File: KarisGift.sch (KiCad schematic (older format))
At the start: 35 parts

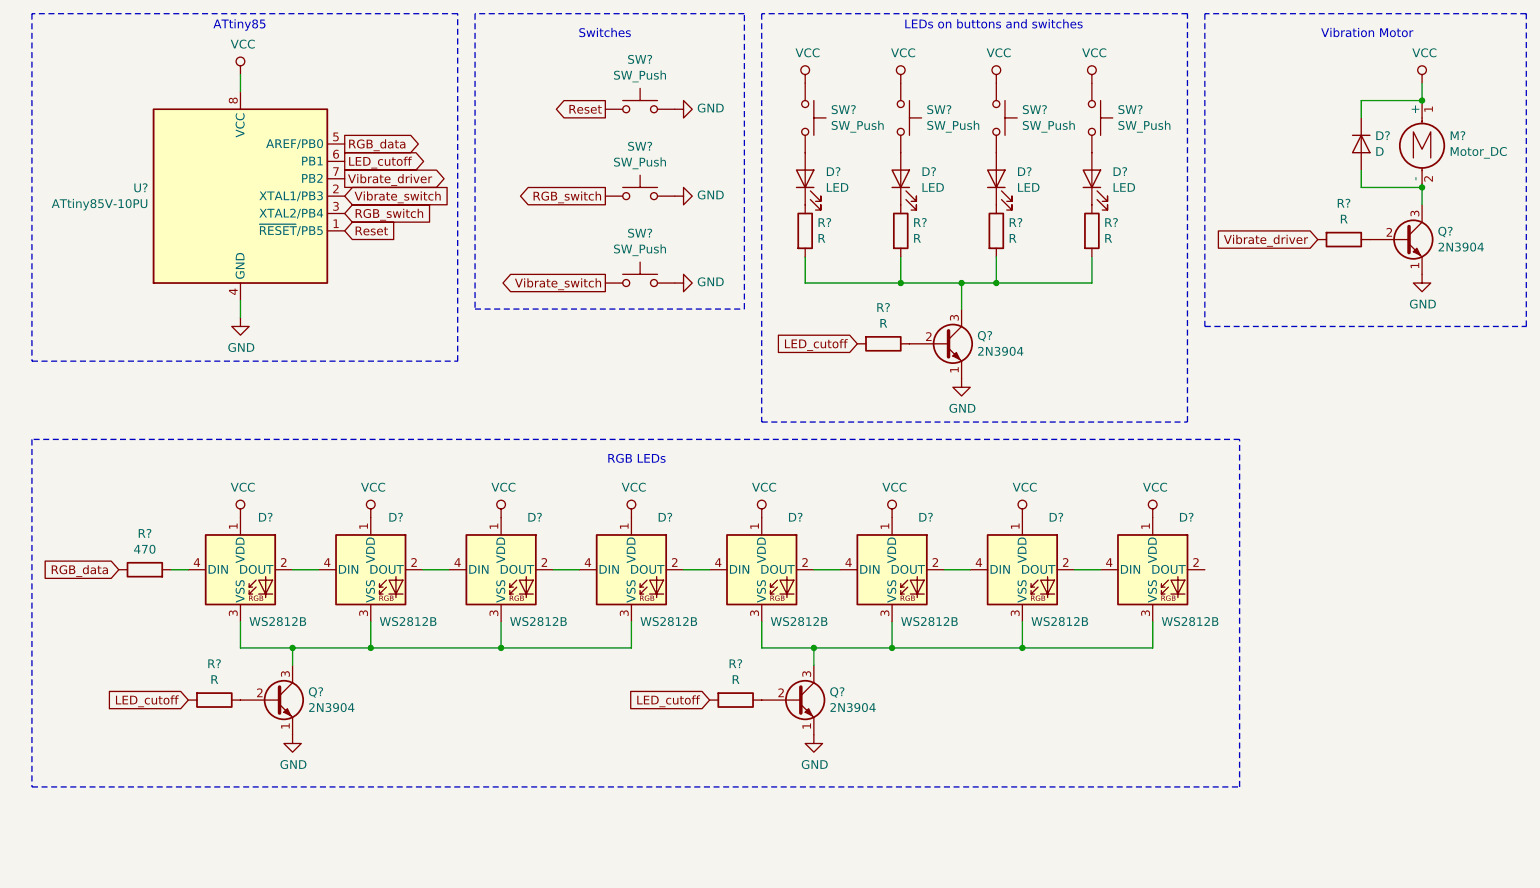
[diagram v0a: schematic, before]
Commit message: Updated RGB LEDs block to not move ground reference on data signal.
Added pull up/down resisters for transistors.
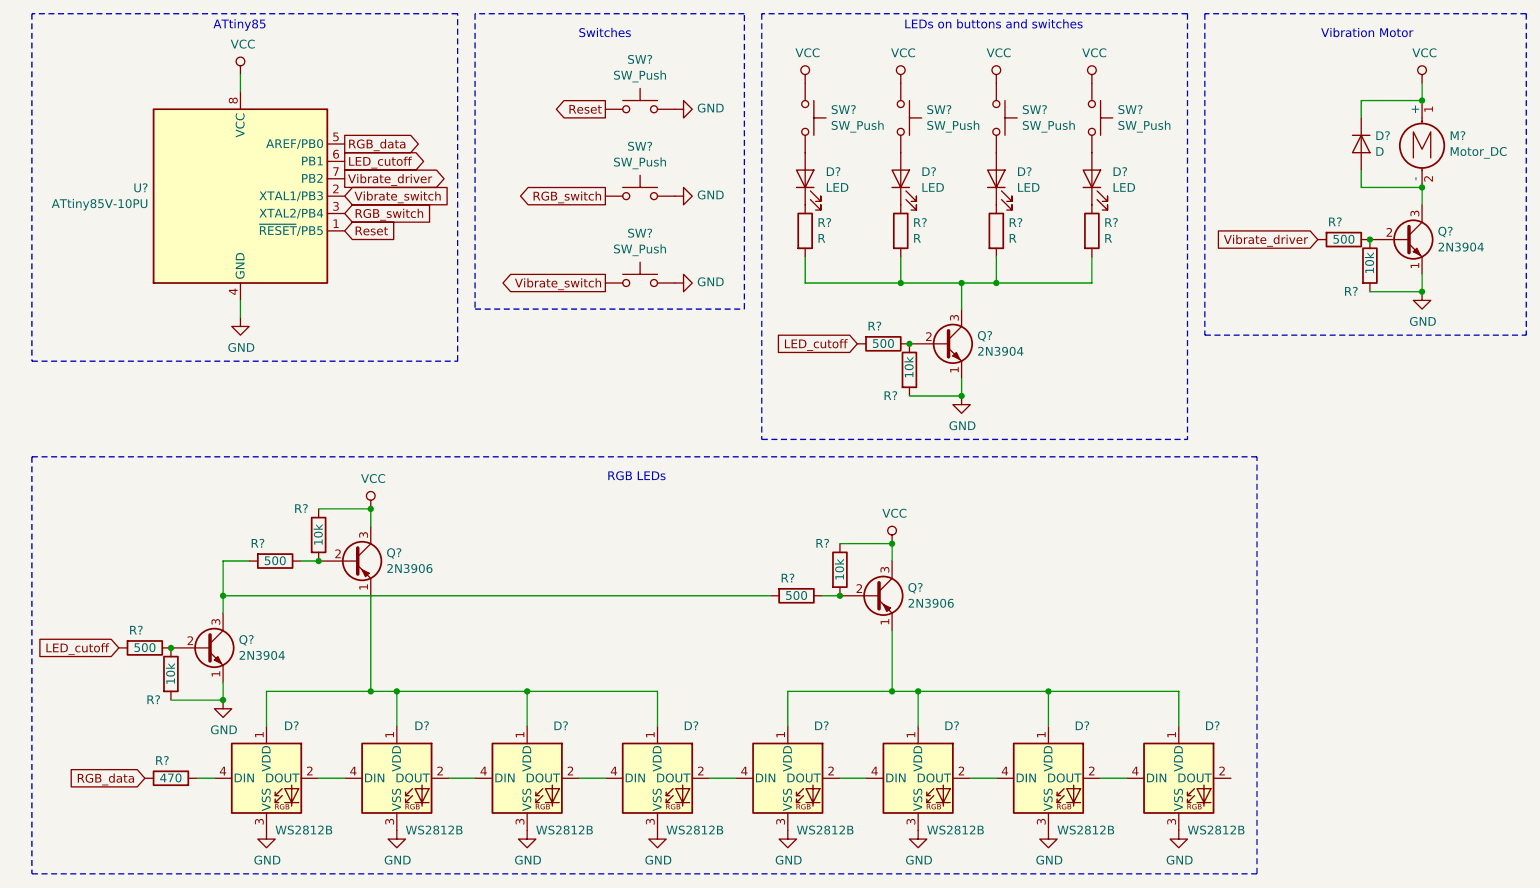
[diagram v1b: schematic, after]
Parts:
- removed Q?: 2N3904, Package_TO_SOT_THT:TO-92_Inline, symbol Transistor_BJT:2N3904
- removed R?: R, symbol Device:R
- added Q? (x2): 2N3906, Package_TO_SOT_THT:TO-92_Inline, symbol Transistor_BJT:2N3906
- added R? (x5): 10k, symbol Device:R
- added R? (x2): 500, symbol Device:R
- R? (x3): value R -> 500
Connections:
- net GND: now also D?.3 (VSS), D?.3 (VSS), D?.3 (VSS), D?.3 (VSS), D?.3 (VSS), D?.3 (VSS), D?.3 (VSS), D?.3 (VSS), R?.2, R?.2, R?.2
- net VCC: now also Q?.3 (C), Q?.3 (C), R?.1, R?.1; no longer D?.1 (VDD), D?.1 (VDD), D?.1 (VDD), D?.1 (VDD), D?.1 (VDD), D?.1 (VDD), D?.1 (VDD), D?.1 (VDD)
- net at Q?.2 (B), R?.1: now also R?.1 (x3)
- new net: D?.1 (VDD), D?.1 (VDD), D?.1 (VDD), D?.1 (VDD), Q?.1 (E) (x2)
- new net: Q?.3 (C), R?.2, R?.2
- new net: Q?.2 (B), R?.1, R?.2 (x2)
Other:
- moved on the sheet: D?, Q?, R?

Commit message: I can't believe it works! The code works!
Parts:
- U?: symbol MCU_Microchip_ATtiny:ATtiny85V-10PU -> KarisGift-rescue:ATtiny85V-10PU-MCU_Microchip_ATtiny
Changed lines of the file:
@@
 EESchema Schematic File Version 4
+LIBS:KarisGift-cache
 EELAYER 30 0
 EELAYER END
@@
 $EndDescr
 $Comp
-L MCU_Microchip_ATtiny:ATtiny85V-10PU U?
+L KarisGift-rescue:ATtiny85V-10PU-MCU_Microchip_ATtiny U?
 U 1 1 5FDE0C7F
 P 1900 1700

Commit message: Updated schematic to use just one PNP transistor for RGB LEDs.
Started the long process of cleaning up the code.
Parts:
- removed Q?: 2N3906, Package_TO_SOT_THT:TO-92_Inline, symbol Transistor_BJT:2N3906
- removed R?: 10k, symbol Device:R
- removed R?: 500, symbol Device:R
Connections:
- net at D?.1 (VDD), D?.1 (VDD), D?.1 (VDD)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: now also D?.1 (VDD), D?.1 (VDD), D?.1 (VDD), D?.1 (VDD)
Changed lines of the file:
@@
 Connection ~ 3550 4550
-$Comp
-L power:VCC #PWR?
-U 1 1 5FFC19B6
-P 5650 3700
-F 0 "#PWR?" H 5650 3550 50  0001 C CNN
-F 1 "VCC" H 5665 3873 50  0000 C CNN
-F 2 "" H 5650 3700 50  0001 C CNN
-F 3 "" H 5650 3700 50  0001 C CNN
-	1    5650 3700
-	1    0    0    -1
-$EndComp
-$Comp
-L Transistor_BJT:2N3906 Q?
-U 1 1 5FFC19BC
-P 5550 4000
-F 0 "Q?" H 5740 4046 50  0000 L CNN
-F 1 "2N3906" H 5740 3955 50  0000 L CNN
-F 2 "Package_TO_SOT_THT:TO-92_Inline" H 5750 3925 50  0001 L CIN
-F 3 "https://www.fairchildsemi.com/datasheets/2N/2N3906.pdf" H 5550 4000 50  0001 L CNN
-	1    5550 4000
-	1    0    0    -1
-$EndComp
-$Comp
-L Device:R R?
-U 1 1 5FFC19C2
-P 5350 3850
-F 0 "R?" H 5250 4000 50  0000 C CNN
-F 1 "10k" V 5350 3850 50  0000 C CNN
-F 2 "" V 5280 3850 50  0001 C CNN
-F 3 "~" H 5350 3850 50  0001 C CNN
-	1    5350 3850
-	1    0    0    -1
-$EndComp
-Wire Wire Line
-	5350 3700 5650 3700
-Wire Wire Line
-	5650 3700 5650 3800
-Connection ~ 5650 3700
-$Comp
-L Device:R R?
-U 1 1 5FFC19CB
-P 5100 4000
-F 0 "R?" V 5000 3950 50  0000 C CNN
-F 1 "500" V 5100 4000 50  0000 C CNN
-F 2 "" V 5030 4000 50  0001 C CNN
-F 3 "~" H 5100 4000 50  0001 C CNN
-	1    5100 4000
-	0    1    1    0
-$EndComp
-Wire Wire Line
-	5350 4000 5250 4000
-Connection ~ 5350 4000
 $Comp
 L power:GND #PWR?
@@
 	7300 4550 7300 4750
 Connection ~ 6550 4550
-Wire Wire Line
-	5050 4550 5650 4550
-Wire Wire Line
-	1800 3800 1800 4000
-Connection ~ 1800 4000
-Wire Wire Line
-	1800 4000 1800 4100
-Wire Wire Line
-	5650 4200 5650 4550
-Connection ~ 5650 4550
-Wire Wire Line
-	5650 4550 5800 4550
 $Comp
 L Device:R R?
@@
 	4900 650  4900 3100
 Wire Wire Line
-	1800 4000 4950 4000
+	5050 4550 5800 4550
+Wire Wire Line
+	1800 3800 1800 4100
+Wire Wire Line
+	5050 4550 4300 4550
+Connection ~ 5050 4550
+Connection ~ 4300 4550
 $EndSCHEMATC

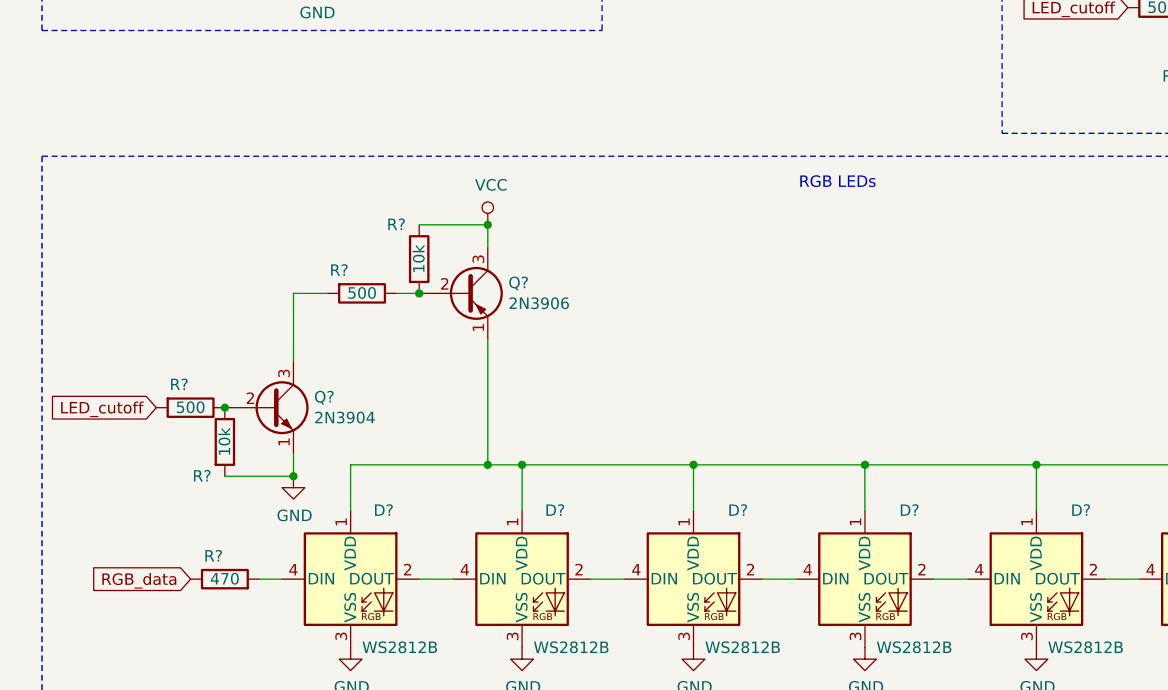
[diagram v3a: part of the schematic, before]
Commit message: Fixed backwards PNP transistor running the RGB LEDs (Thanks Ron!)
Some more code cleanup.
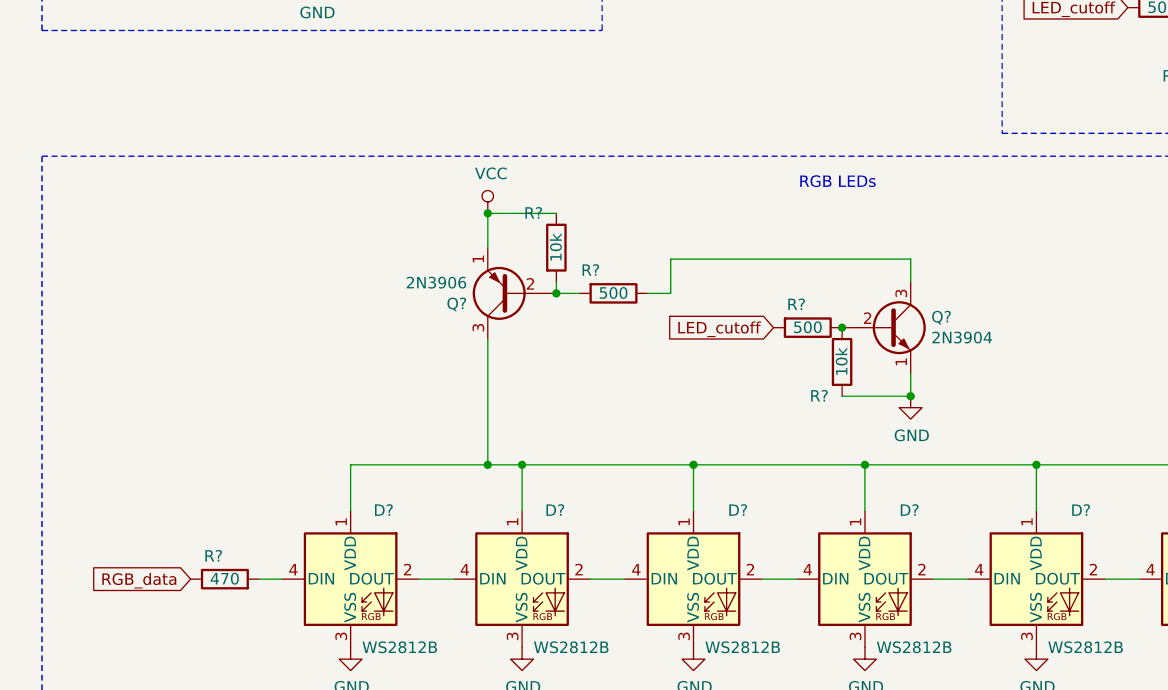
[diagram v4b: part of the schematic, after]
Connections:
- net VCC: now also Q?.1 (E); no longer Q?.3 (C)
- net at D?.1 (VDD), D?.1 (VDD), D?.1 (VDD)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: now also Q?.3 (C); no longer Q?.1 (E)
- net at Q?.3 (C): now also R?.1; no longer R?.2
- net at Q?.2 (B), R?.2: now also R?.2; no longer R?.1
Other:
- moved on the sheet: Q?, R?
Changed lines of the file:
@@
 L power:VCC #PWR?
 U 1 1 5FE03943
-P 2650 3500
-F 0 "#PWR?" H 2650 3350 50  0001 C CNN
-F 1 "VCC" H 2665 3673 50  0000 C CNN
-F 2 "" H 2650 3500 50  0001 C CNN
-F 3 "" H 2650 3500 50  0001 C CNN
-	1    2650 3500
+P 2650 3450
+F 0 "#PWR?" H 2650 3300 50  0001 C CNN
+F 1 "VCC" H 2665 3623 50  0000 C CNN
+F 2 "" H 2650 3450 50  0001 C CNN
+F 3 "" H 2650 3450 50  0001 C CNN
+	1    2650 3450
 	1    0    0    -1
 $EndComp
@@
 L Device:R R?
 U 1 1 5FE0932F
-P 1350 4300
-F 0 "R?" V 1250 4250 50  0000 C CNN
-F 1 "500" V 1350 4300 50  0000 C CNN
-F 2 "" V 1280 4300 50  0001 C CNN
-F 3 "~" H 1350 4300 50  0001 C CNN
-	1    1350 4300
+P 4050 3950
+F 0 "R?" V 3950 3900 50  0000 C CNN
+F 1 "500" V 4050 3950 50  0000 C CNN
+F 2 "" V 3980 3950 50  0001 C CNN
+F 3 "~" H 4050 3950 50  0001 C CNN
+	1    4050 3950
 	0    1    1    0
 $EndComp
@@
 L power:GND #PWR?
 U 1 1 5FE09335
-P 1800 4600
-F 0 "#PWR?" H 1800 4350 50  0001 C CNN
-F 1 "GND" H 1805 4427 50  0000 C CNN
-F 2 "" H 1800 4600 50  0001 C CNN
-F 3 "" H 1800 4600 50  0001 C CNN
-	1    1800 4600
+P 4500 4250
+F 0 "#PWR?" H 4500 4000 50  0001 C CNN
+F 1 "GND" H 4505 4077 50  0000 C CNN
+F 2 "" H 4500 4250 50  0001 C CNN
+F 3 "" H 4500 4250 50  0001 C CNN
+	1    4500 4250
 	1    0    0    -1
 $EndComp
@@
 Wire Wire Line
 	1650 5050 1750 5050
-Text GLabel 1200 4300 0    50   Input ~ 0
+Text GLabel 3900 3950 0    50   Input ~ 0
 LED_cutoff
 Text Notes 4350 3350 2    50   ~ 0
@@
 L Transistor_BJT:2N3904 Q?
 U 1 1 5FE09329
-P 1700 4300
-F 0 "Q?" H 1890 4346 50  0000 L CNN
-F 1 "2N3904" H 1890 4255 50  0000 L CNN
-F 2 "Package_TO_SOT_THT:TO-92_Inline" H 1900 4225 50  0001 L CIN
-F 3 "https://www.fairchildsemi.com/datasheets/2N/2N3904.pdf" H 1700 4300 50  0001 L CNN
-	1    1700 4300
+P 4400 3950
+F 0 "Q?" H 4590 3996 50  0000 L CNN
+F 1 "2N3904" H 4590 3905 50  0000 L CNN
+F 2 "Package_TO_SOT_THT:TO-92_Inline" H 4600 3875 50  0001 L CIN
+F 3 "https://www.fairchildsemi.com/datasheets/2N/2N3904.pdf" H 4400 3950 50  0001 L CNN
+	1    4400 3950
 	1    0    0    -1
 $EndComp
@@
 L Transistor_BJT:2N3906 Q?
 U 1 1 5FFA5010
-P 2550 3800
-F 0 "Q?" H 2740 3846 50  0000 L CNN
-F 1 "2N3906" H 2740 3755 50  0000 L CNN
-F 2 "Package_TO_SOT_THT:TO-92_Inline" H 2750 3725 50  0001 L CIN
-F 3 "https://www.fairchildsemi.com/datasheets/2N/2N3906.pdf" H 2550 3800 50  0001 L CNN
-	1    2550 3800
-	1    0    0    -1
+P 2750 3800
+F 0 "Q?" H 2940 3846 50  0000 L CNN
+F 1 "2N3906" H 2940 3755 50  0000 L CNN
+F 2 "Package_TO_SOT_THT:TO-92_Inline" H 2950 3725 50  0001 L CIN
+F 3 "https://www.fairchildsemi.com/datasheets/2N/2N3906.pdf" H 2750 3800 50  0001 L CNN
+	1    2750 3800
+	-1   0    0    1
 $EndComp
 $Comp
 L Device:R R?
 U 1 1 5FFA603B
-P 2350 3650
-F 0 "R?" H 2250 3800 50  0000 C CNN
-F 1 "10k" V 2350 3650 50  0000 C CNN
-F 2 "" V 2280 3650 50  0001 C CNN
-F 3 "~" H 2350 3650 50  0001 C CNN
-	1    2350 3650
-	1    0    0    -1
-$EndComp
-Wire Wire Line
-	2350 3500 2650 3500
-Wire Wire Line
-	2650 3500 2650 3600
-Connection ~ 2650 3500
+P 2950 3600
+F 0 "R?" H 2850 3750 50  0000 C CNN
+F 1 "10k" V 2950 3600 50  0000 C CNN
+F 2 "" V 2880 3600 50  0001 C CNN
+F 3 "~" H 2950 3600 50  0001 C CNN
+	1    2950 3600
+	1    0    0    -1
+$EndComp
 $Comp
 L Device:R R?
 U 1 1 5FFAFFBD
-P 2100 3800
-F 0 "R?" V 2000 3700 50  0000 C CNN
-F 1 "500" V 2100 3800 50  0000 C CNN
-F 2 "" V 2030 3800 50  0001 C CNN
-F 3 "~" H 2100 3800 50  0001 C CNN
-	1    2100 3800
+P 3200 3800
+F 0 "R?" V 3100 3700 50  0000 C CNN
+F 1 "500" V 3200 3800 50  0000 C CNN
+F 2 "" V 3130 3800 50  0001 C CNN
+F 3 "~" H 3200 3800 50  0001 C CNN
+	1    3200 3800
 	0    1    1    0
 $EndComp
-Wire Wire Line
-	2350 3800 2250 3800
-Connection ~ 2350 3800
-Wire Wire Line
-	1950 3800 1800 3800
 $Comp
 L power:GND #PWR?
@@
 L Device:R R?
 U 1 1 5FFDCB12
-P 1500 4450
-F 0 "R?" H 1400 4300 50  0000 C CNN
-F 1 "10k" V 1500 4450 50  0000 C CNN
-F 2 "" V 1430 4450 50  0001 C CNN
-F 3 "~" H 1500 4450 50  0001 C CNN
-	1    1500 4450
-	1    0    0    -1
-$EndComp
-Connection ~ 1500 4300
-Wire Wire Line
-	1500 4600 1800 4600
-Wire Wire Line
-	1800 4500 1800 4600
-Connection ~ 1800 4600
+P 4200 4100
+F 0 "R?" H 4100 3950 50  0000 C CNN
+F 1 "10k" V 4200 4100 50  0000 C CNN
+F 2 "" V 4130 4100 50  0001 C CNN
+F 3 "~" H 4200 4100 50  0001 C CNN
+	1    4200 4100
+	1    0    0    -1
+$EndComp
+Connection ~ 4200 3950
+Wire Wire Line
+	4200 4250 4500 4250
+Wire Wire Line
+	4500 4150 4500 4250
+Connection ~ 4500 4250
 Wire Notes Line
 	700  5600 7750 5600
@@
 	5050 4550 5800 4550
 Wire Wire Line
-	1800 3800 1800 4100
-Wire Wire Line
 	5050 4550 4300 4550
 Connection ~ 5050 4550
 Connection ~ 4300 4550
+Wire Wire Line
+	2950 3450 2650 3450
+Connection ~ 2650 3450
+Wire Wire Line
+	2650 3450 2650 3600
+Wire Wire Line
+	2950 3750 2950 3800
+Wire Wire Line
+	2950 3800 3050 3800
+Connection ~ 2950 3800
+Wire Wire Line
+	3350 3800 3450 3800
+Wire Wire Line
+	3450 3800 3450 3650
+Wire Wire Line
+	3450 3650 4500 3650
+Wire Wire Line
+	4500 3650 4500 3750
 $EndSCHEMATC
